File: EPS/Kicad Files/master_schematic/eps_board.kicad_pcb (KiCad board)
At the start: 2 copper layers, 96 x 90 mm, 25 parts, among them J1 THD-20-R

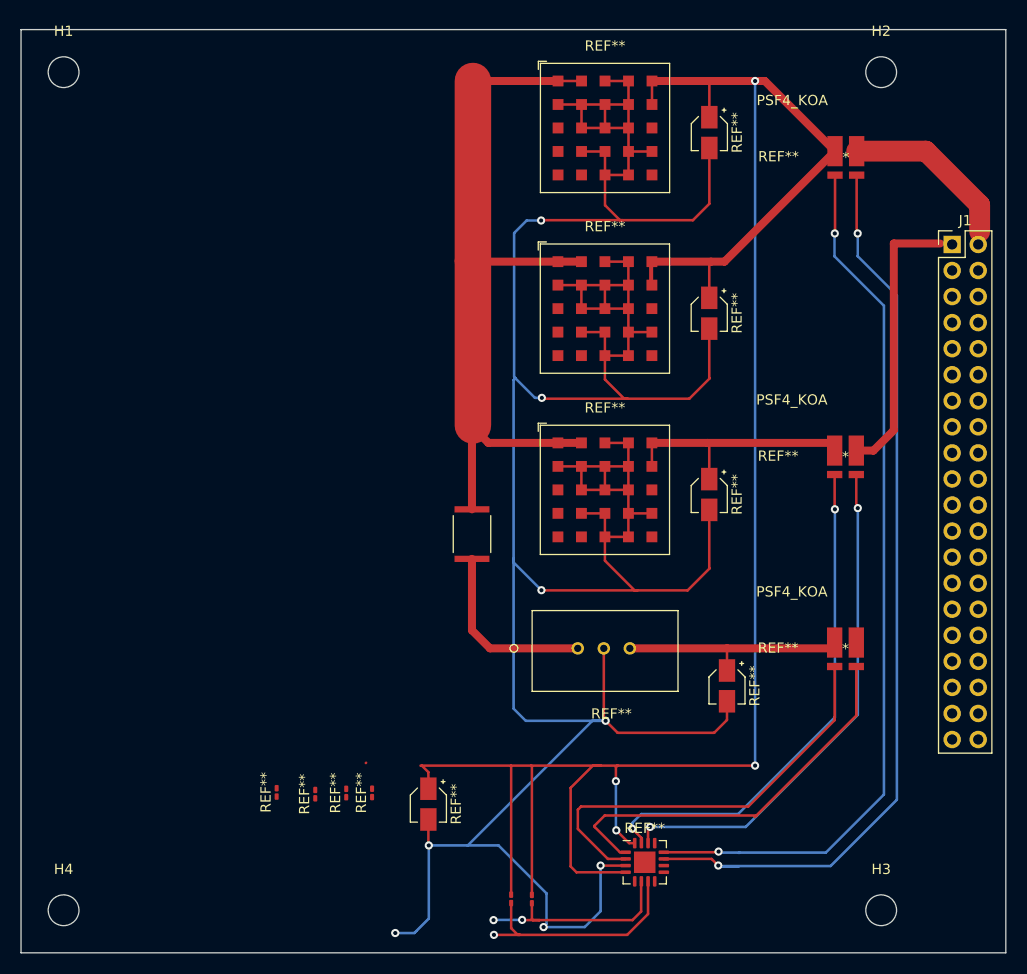
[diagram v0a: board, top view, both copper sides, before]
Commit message: master schematic/pcb update
updates schematic with OVP and added OVP to the PCB layout
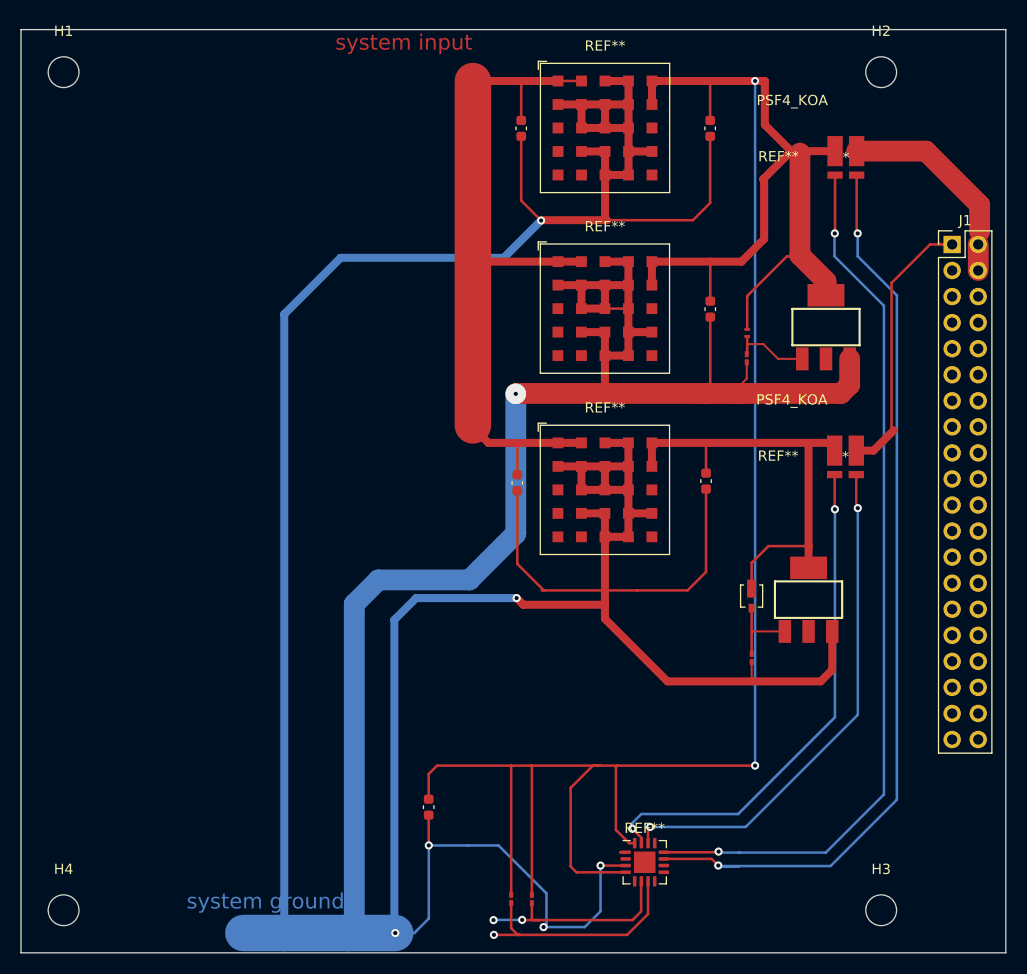
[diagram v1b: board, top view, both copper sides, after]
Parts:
- removed the REF** at (100.4, 80.4)
- removed the REF** at (88.8, 84.0)
- removed the REF** at (87.1, 30.0)
- removed the REF** at (48.7, 94.5)
- removed the REF** at (74.3, 80.3)
- removed the REF** at (59.7, 95.5)
- removed the REF** at (87.1, 47.6)
- removed the REF** at (51.7, 94.4)
- removed the REF** at (54.2, 94.4)
- removed the REF** at (87.1, 65.3)
- removed ptc_fuse: FUS_MINISMDC075F_TYCO_TYC, footprints:MINISMDC075F-2
- added REF**: C_0603_1608Metric, Capacitor_SMD:C_0603_1608Metric, F.Cu at (59.7, 95.8)
- added REF**: C_0603_1608Metric, Capacitor_SMD:C_0603_1608Metric, F.Cu at (87.2, 29.6)
- added REF**: R_0201_0603Metric_Pad0.64x0.40mm_HandSolder, Resistor_SMD:R_0201_0603Metric_Pad0.64x0.40mm_HandSolder, F.Cu at (90.8, 52.0)
- added REF**: C_0603_1608Metric, Capacitor_SMD:C_0603_1608Metric, F.Cu at (87.2, 47.2)
- added REF**: PowerDI323_DIO, 3.6zener:PD3Z284C3V6-7, F.Cu at (91.2, 75.2)
- added REF**: SOT230P700X180-4N, fzt688bta_footprint:SOT230P700X180-4N, F.Cu at (98.5, 49.0)
- added REF**: CR_1L-HG3-08_VIS, 5.1zener:BZX884B5V1L-HG3-08, F.Cu at (90.8, 49.6)
- added REF**: C_0603_1608Metric, Capacitor_SMD:C_0603_1608Metric, F.Cu at (86.8, 64.0)
- added REF**: C_0603_1608Metric, Capacitor_SMD:C_0603_1608Metric, F.Cu at (68.4, 64.2)
- added REF**: SOT230P700X180-4N, fzt688bta_footprint:SOT230P700X180-4N, F.Cu at (96.8, 75.6)
- added REF**: C_0603_1608Metric, Capacitor_SMD:C_0603_1608Metric, F.Cu at (68.8, 29.6)
- moved REF** 48.1 mm to (91.2, 81.2)
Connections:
- REF** pad 1: (no net) -> +5V
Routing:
- net (no net): track 1094.7 -> 1233.6 mm, vias 23 -> 20
- net +5V: track 17.4 -> 20.0 mm
- net +3.3V: track 27.3 -> 26.5 mm
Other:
- board text added: "system ground"
- board text added: "system input"
